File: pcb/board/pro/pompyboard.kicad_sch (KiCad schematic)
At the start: 17 parts, among them J1 USB_C_Receptacle_USB2.0_16P, J2 Conn_01x04_Pin, SW1 EVQQ2B03W, SW2 EVQQ2B03W, U229 STM32F429IGT6, U231 TPS62152

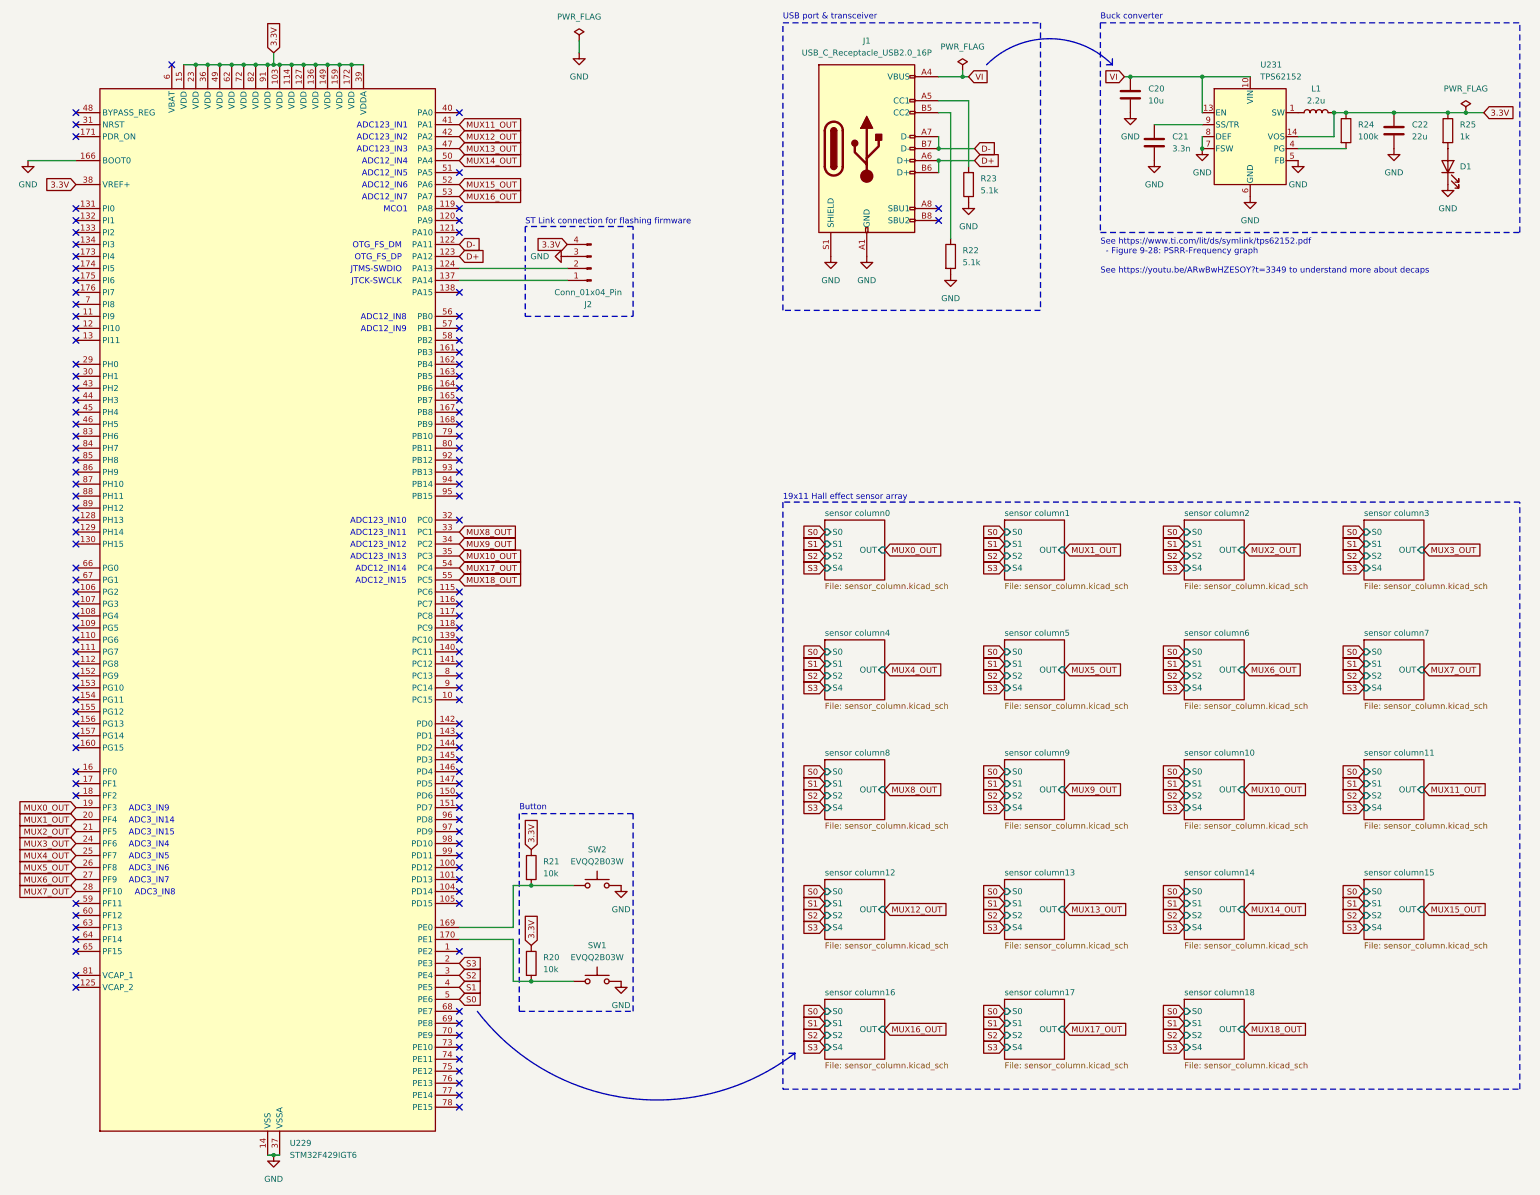
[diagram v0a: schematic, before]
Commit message: Updated with filter caps
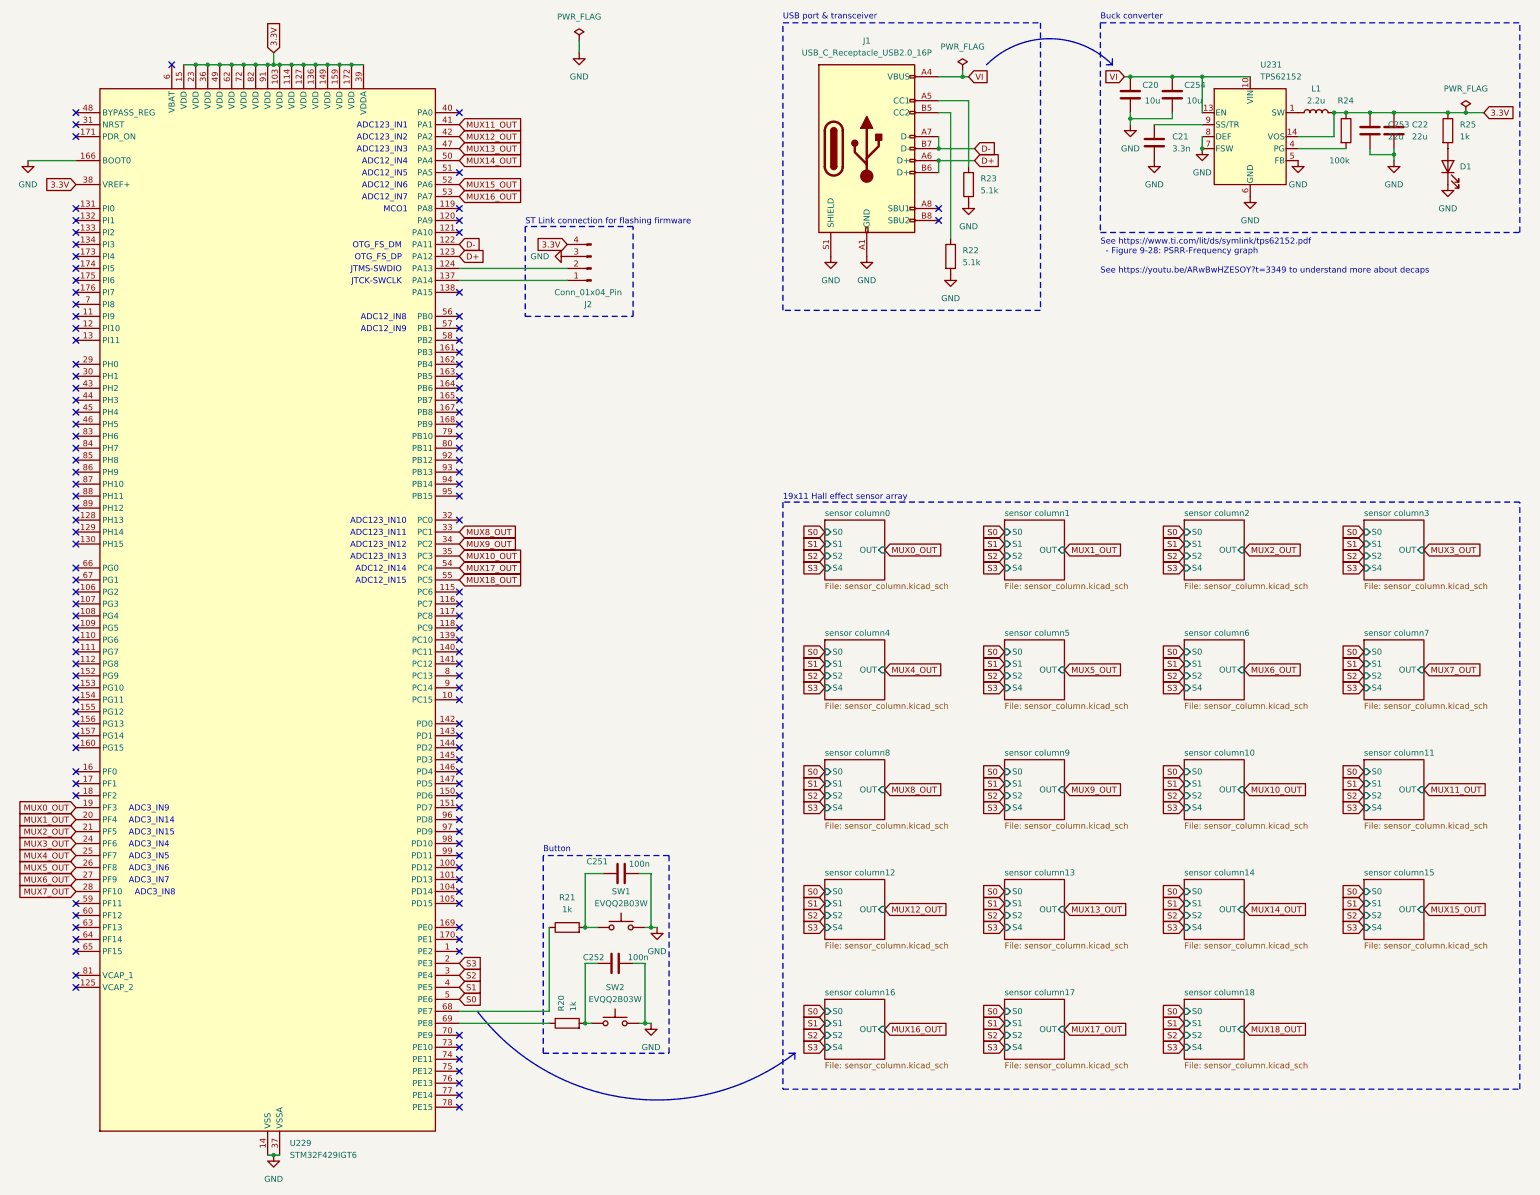
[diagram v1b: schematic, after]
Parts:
- added C251, C252: 100n, Capacitor_SMD:C_0402_1005Metric, symbol Device:C
- added C253: 22u, Capacitor_SMD:C_0402_1005Metric, symbol Device:C
- added C254: 10u, Capacitor_SMD:C_0402_1005Metric, symbol Device:C
- R20: renamed from R21; value 10k -> 1k
- R21: renamed from R20; value 10k -> 1k
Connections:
- net 3.3V: now also C253.1; no longer R20.1, R21.1
- net GND: now also C251.2, C252.2, C253.2, C254.2
- net VI: now also C254.1
- net at R21.2, SW1.1: now also C251.1; no longer U229.170 (PE1)
- net at R20.2, SW2.1: now also C252.1; no longer U229.169 (PE0)
- net at U229.68 (PE7): now also R21.1
- net at U229.69 (PE8): now also R20.1
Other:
- moved on the sheet: R20, R21, SW1, SW2
